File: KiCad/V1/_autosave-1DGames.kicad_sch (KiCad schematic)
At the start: 13 parts, among them J1 TM1637 Four Digits Led Displa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, Q1 AO3401A, Q2 AO3401A, U1 ESP32-DEVKITC-32D

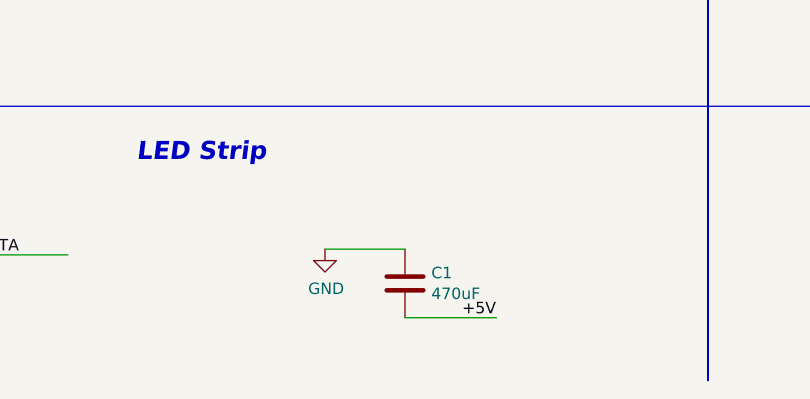
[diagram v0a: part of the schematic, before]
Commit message: Electronic scheme, program for calculating LED coordinates.
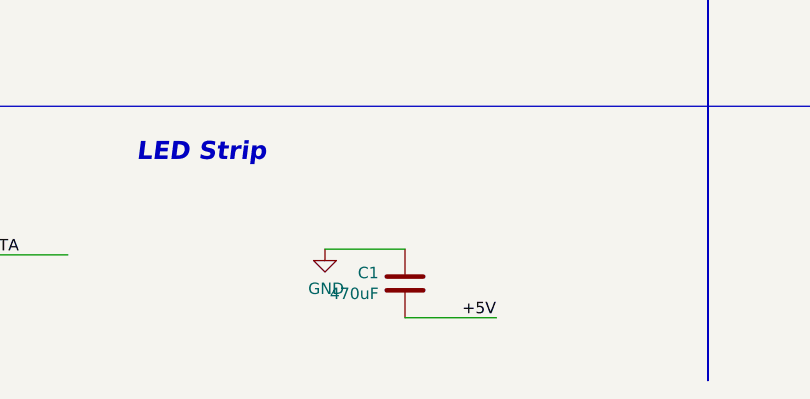
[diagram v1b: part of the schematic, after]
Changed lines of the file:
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@@
     (pin "1")
   )
-  (symbol (lib_id "Device:C") (at 93.98 185.42 0) (unit 1)
+  (symbol (lib_id "Device:C") (at 93.98 185.42 0) (mirror y) (unit 1)
     (in_bom yes) (on_board yes)
-    (property "Reference" "C1" (id 0) (at 96.901 184.2516 0)
+    (property "Reference" "C1" (id 0) (at 91.059 184.2516 0)
       (effects (font (size 1.27 1.27)) (justify left))
     )
-    (property "Value" "470uF" (id 1) (at 96.901 186.563 0)
+    (property "Value" "470uF" (id 1) (at 91.059 186.563 0)
       (effects (font (size 1.27 1.27)) (justify left))
     )
-    (property "Footprint" "Capacitor_THT:CP_Radial_D5.0mm_P2.50mm" (id 2) (at 96.901 187.7314 0)
+    (property "Footprint" "Capacitor_THT:CP_Radial_D5.0mm_P2.50mm" (id 2) (at 91.059 187.7314 0)
       (effects (font (size 1.27 1.27)) (justify left) hide)
     )
